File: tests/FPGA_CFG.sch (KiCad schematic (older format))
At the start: 5 parts, among them U4 iCE40-HX8K-CT256, U6 SPI Flash

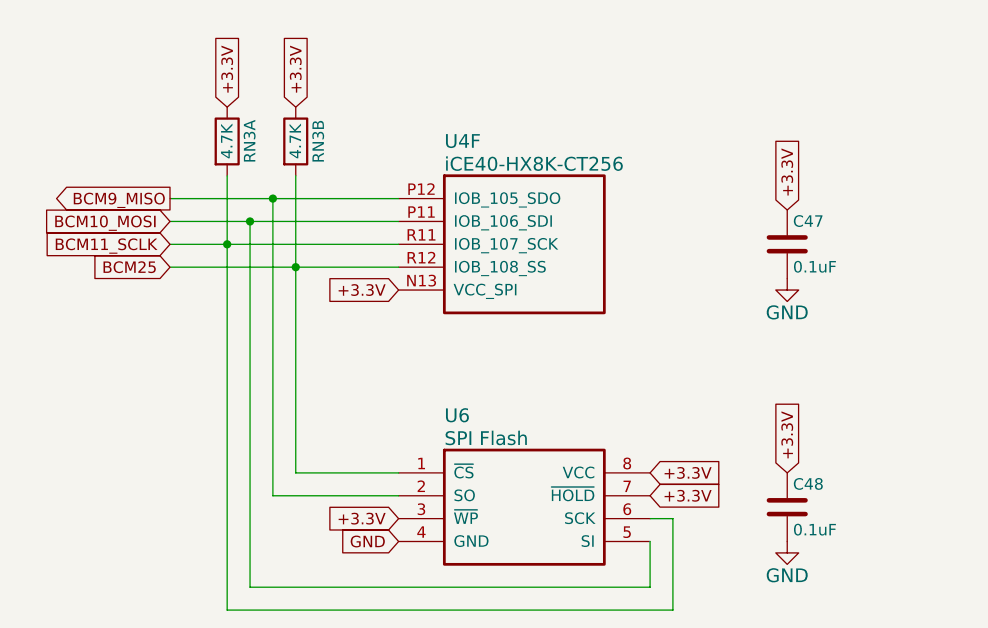
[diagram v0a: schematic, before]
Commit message: Added recursive operations on hierarchical schematics.
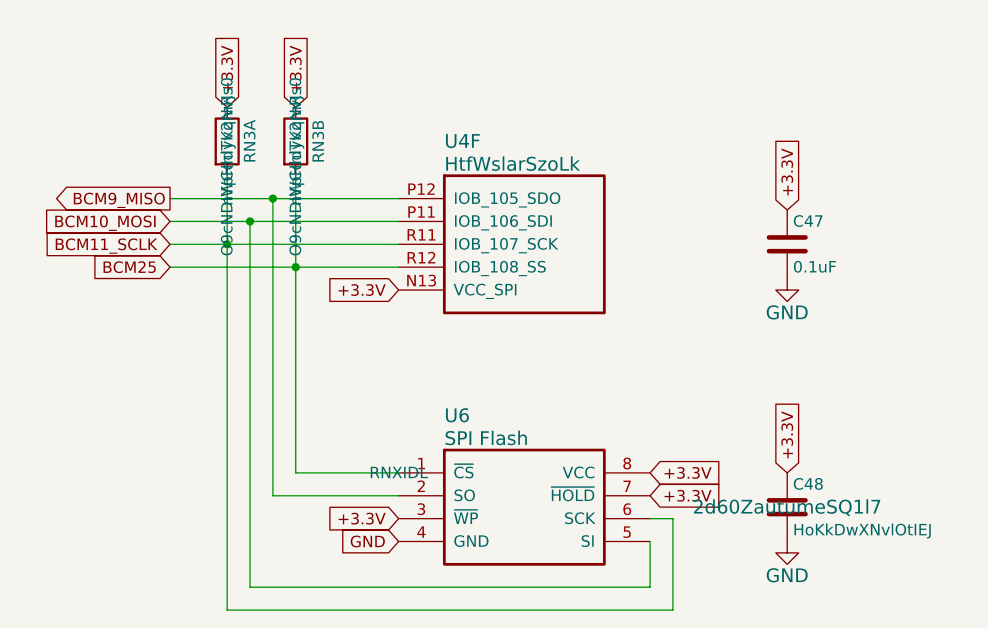
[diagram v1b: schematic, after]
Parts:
- C48: value 0.1uF -> HoKkDwXNvlOtIEJ; manf (none) -> wgv1k7Mtrqu4FiUuJ; zzzky (none) -> YwKtaTHS7T5qhu6uO
- RN3: value 4.7K -> nYpHnIyv2mRs0
- U4: value iCE40-HX8K-CT256 -> HtfWslarSzoLk; manf# (none) -> HiyQG6ncOK
- U6: footprint SMD_Packages:SOIC-8-N -> ZGw0Xf; manf (none) -> ApinVpn3SOcHzWlMcpv
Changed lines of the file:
@@
 AR Path="/55F04F56" Ref="U?" Part="6"
 F 0 "U4" H 5800 3750 60 0000 L CNN
-F 1 "iCE40-HX8K-CT256" H 5800 3650 60 0000 L CNN
+F 1 "HtfWslarSzoLk" H 5800 3650 60 0000 L CNN
 F 2 "XESS:Lattice_caBGA_256" H 5600 3500 60 0001 C CNN
 F 3 "" H 5600 3500 60 0000 C CNN
+F 4 "HiyQG6ncOK" H 0 0 50 0001 C CNN "manf#"
 	6    5600 3500
 	1    0    0    -1
@@
 F 0 "U6" H 5800 4950 60 0000 L CNN
 F 1 "SPI Flash" H 5800 4850 60 0000 L CNN
-F 2 "SMD_Packages:SOIC-8-N" H 5600 4700 50 0001 C CNN
-F 3 "" H 5600 4700 50 0000 C CNN
-F 4 "AT25SF041-SSHD-T" H 5600 4700 60 0001 C CNN "manf#"
-F 5 "" H 0 0 50 0001 C CNN "manf"
+F 2 "ZGw0Xf" H 5600 4700 50 0001 C CNN
+F 3 "RNXIDL" H 5600 4700 50 0000 C CNN
+F 4 "ApinVpn3SOcHzWlMcpv" H 0 0 50 0001 C CNN "manf"
+F 5 "AT25SF041-SSHD-T" H 5600 4700 60 0001 C CNN "manf#"
 	1    5600 4700
 	1    0    0    -1
@@
 F 2 "Capacitors_SMD:C_0603" H 7338 3550 30 0001 C CNN
 F 3 "" H 7300 3700 60 0000 C CNN
-F 4 "" H 0 0 50 0001 C CNN "manf#"
-F 5 "" H 0 0 50 0001 C CNN "manf"
 	1    7300 3700
 	1    0    0    -1
@@
 P 7300 4850
 F 0 "C48" H 7325 4950 50 0000 L CNN
-F 1 "0.1uF" H 7325 4750 50 0000 L CNN
+F 1 "HoKkDwXNvlOtIEJ" H 7325 4750 50 0000 L CNN
 F 2 "Capacitors_SMD:C_0603" H 7338 4700 30 0001 C CNN
-F 3 "" H 7300 4850 60 0000 C CNN
-F 4 "" H 0 0 50 0001 C CNN "manf#"
-F 5 "" H 0 0 50 0001 C CNN "manf"
+F 3 "2d60ZautumeSQ1l7" H 7300 4850 60 0000 C CNN
+F 4 "wgv1k7Mtrqu4FiUuJ" H 0 0 50 0001 C CNN "manf"
+F 5 "YwKtaTHS7T5qhu6uO" H 0 0 50 0001 C CNN "zzzky"
 	1    7300 4850
 	1    0    0    -1
@@
 P 4850 3400
 F 0 "RN3" H 5000 3300 50 0000 C CNN
-F 1 "4.7K" H 5000 3400 50 0000 C CNN
+F 1 "nYpHnIyv2mRs0" H 5000 3400 50 0000 C CNN
 F 2 "XESS:CTS_742C043" H 4850 3400 50 0001 C CNN
-F 3 "" H 4850 3400 50 0000 C CNN
-F 4 "" H 0 0 50 0001 C CNN "manf#"
-F 5 "" H 0 0 50 0001 C CNN "manf"
+F 3 "O9cNDIWCddTKqNvJ" H 4850 3400 50 0000 C CNN
 	1    4850 3400
 	0    -1   -1   0
@@
 P 5150 3400
 F 0 "RN3" H 5300 3300 50 0000 C CNN
-F 1 "4.7K" H 5300 3400 50 0000 C CNN
+F 1 "nYpHnIyv2mRs0" H 5300 3400 50 0000 C CNN
 F 2 "XESS:CTS_742C043" H 5150 3400 50 0001 C CNN
-F 3 "" H 5150 3400 50 0000 C CNN
-F 4 "" H 0 0 50 0001 C CNN "manf#"
-F 5 "" H 0 0 50 0001 C CNN "manf"
+F 3 "O9cNDIWCddTKqNvJ" H 5150 3400 50 0000 C CNN
 	2    5150 3400
 	0    -1   -1   0
